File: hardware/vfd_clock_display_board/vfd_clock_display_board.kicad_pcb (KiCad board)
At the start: 2 copper layers, 124.9 x 94.6 mm, 96 parts, among them J1 Conn_01x12_Pin, Q1 MMDT5551, Q10 2N3906, Q11 2N3906, Q12 2N3906, Q13 MMDT5551, Q14 MMDT5551, Q15 2N3906, Q16 2N3906, Q17 2N3906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

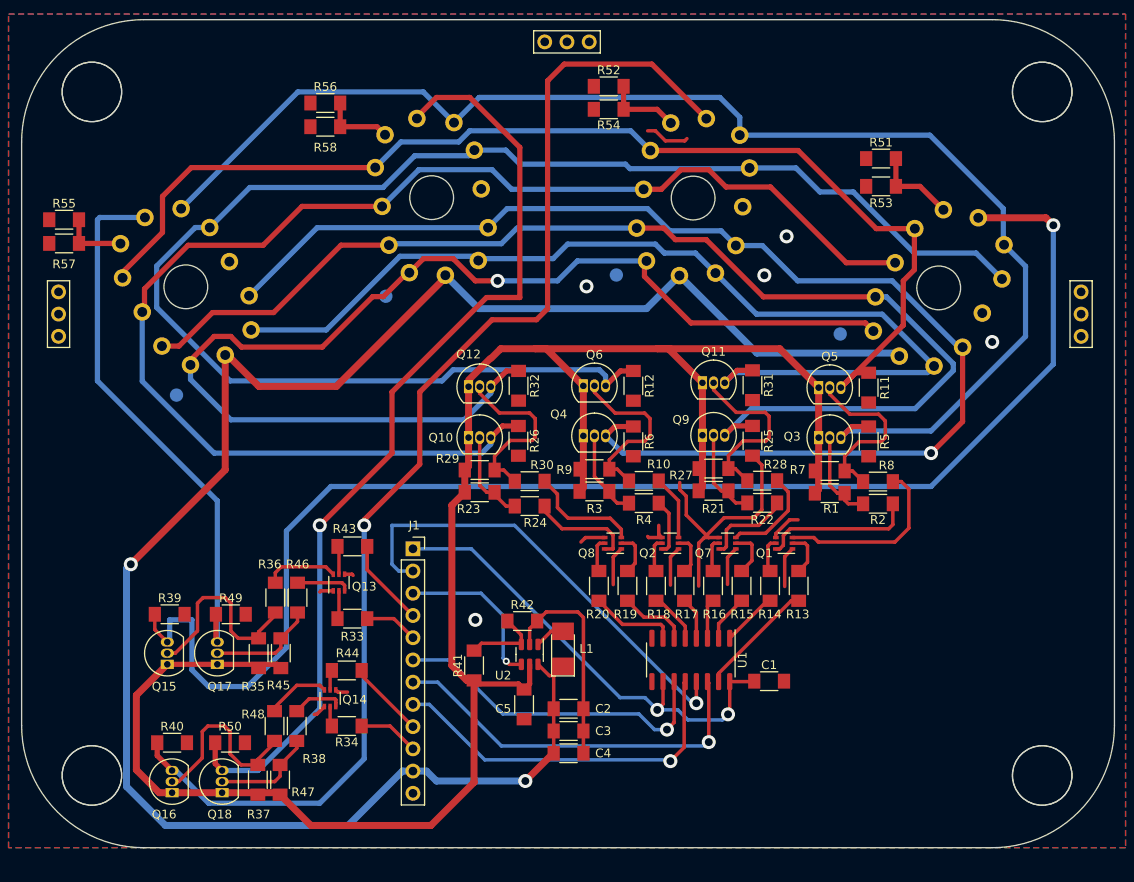
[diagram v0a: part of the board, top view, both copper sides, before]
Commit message: Add PCF version of main board, add test pads to display board
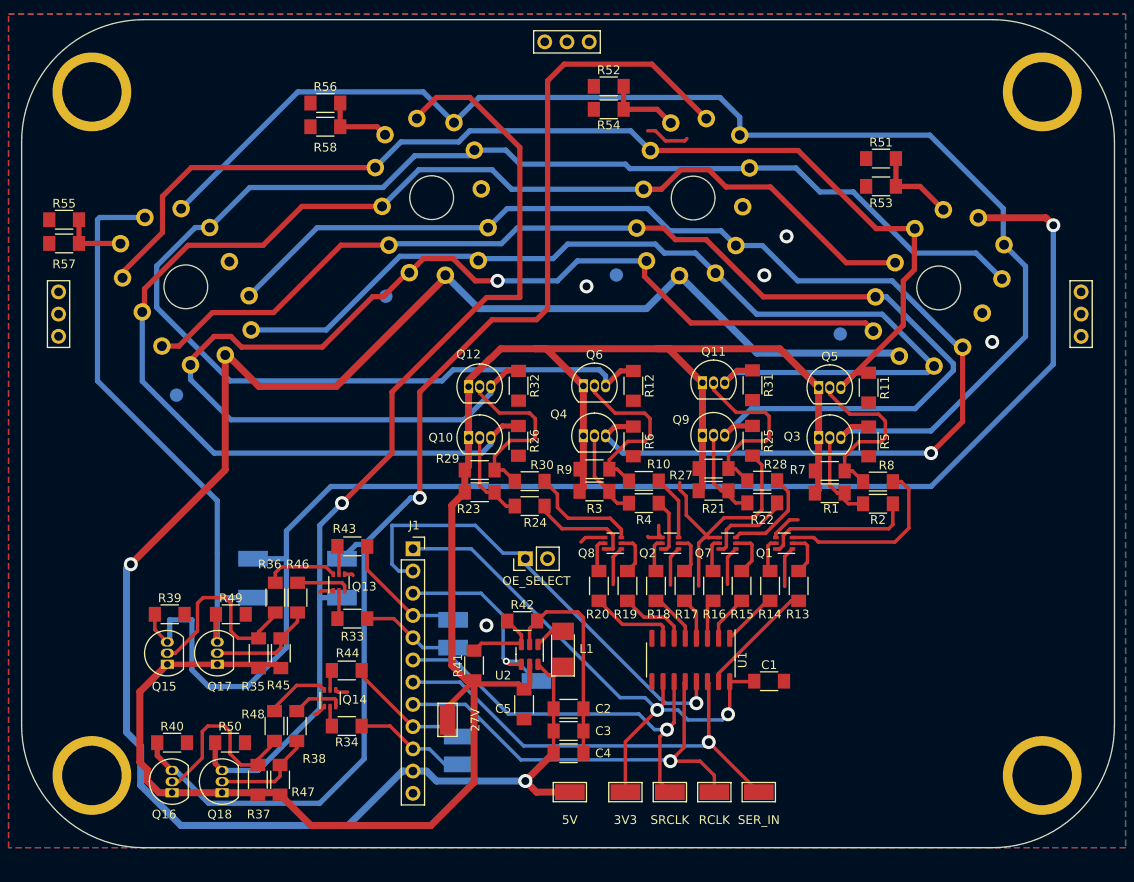
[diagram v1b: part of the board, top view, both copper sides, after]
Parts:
- added 27V: TestPoint_Keystone_5015_Micro-Minature, TestPoint:TestPoint_Keystone_5015_Micro-Minature, F.Cu at (139.1, 135.3)
- added 3V3: TestPoint_Keystone_5015_Micro-Minature, TestPoint:TestPoint_Keystone_5015_Micro-Minature, F.Cu at (159.4, 143.5)
- added 5V: TestPoint_Keystone_5015_Micro-Minature, TestPoint:TestPoint_Keystone_5015_Micro-Minature, F.Cu at (153.0, 143.5)
- added OE_SELECT: Conn_01x02_Pin, Connector_PinHeader_2.54mm:PinHeader_1x02_P2.54mm_Vertical, F.Cu at (147.9, 116.8)
- added RCLK: TestPoint_Keystone_5015_Micro-Minature, TestPoint:TestPoint_Keystone_5015_Micro-Minature, F.Cu at (169.5, 143.5)
- added SER_IN: TestPoint_Keystone_5015_Micro-Minature, TestPoint:TestPoint_Keystone_5015_Micro-Minature, F.Cu at (174.6, 143.5)
- added SRCLK: TestPoint_Keystone_5015_Micro-Minature, TestPoint:TestPoint_Keystone_5015_Micro-Minature, F.Cu at (164.5, 143.5)
- added TLV_EN: TestPoint_Keystone_5015_Micro-Minature, TestPoint:TestPoint_Keystone_5015_Micro-Minature, B.Cu at (149.2, 130.8)
- added VFD0_EN: TestPoint_Keystone_5015_Micro-Minature, TestPoint:TestPoint_Keystone_5015_Micro-Minature, B.Cu at (139.7, 127.0)
- added VFD0_GRID: TestPoint_Keystone_5015_Micro-Minature, TestPoint:TestPoint_Keystone_5015_Micro-Minature, B.Cu at (116.8, 116.8)
- added VFD1_EN: TestPoint_Keystone_5015_Micro-Minature, TestPoint:TestPoint_Keystone_5015_Micro-Minature, B.Cu at (139.7, 123.8)
- added VFD1_EN: TestPoint_Keystone_5015_Micro-Minature, TestPoint:TestPoint_Keystone_5015_Micro-Minature, B.Cu at (140.3, 137.2)
- added VFD1_EN: TestPoint_Keystone_5015_Micro-Minature, TestPoint:TestPoint_Keystone_5015_Micro-Minature, B.Cu at (140.3, 140.3)
- added VFD1_GRID: TestPoint_Keystone_5015_Micro-Minature, TestPoint:TestPoint_Keystone_5015_Micro-Minature, B.Cu at (116.8, 121.3)
- added VFD2_GRID: TestPoint_Keystone_5015_Micro-Minature, TestPoint:TestPoint_Keystone_5015_Micro-Minature, B.Cu at (127.0, 116.8)
- added VFD3_GRID: TestPoint_Keystone_5015_Micro-Minature, TestPoint:TestPoint_Keystone_5015_Micro-Minature, B.Cu at (127.0, 121.3)
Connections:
- ? pad : (no net) -> PWR_GND (x4)
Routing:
- net PWR_3V3: track 54.5 -> 65.4 mm
- net /SER_IN: track 44.0 -> 52.1 mm
- net /SRCLK: track 38.1 -> 46.1 mm
- net /RCLK: track 41.9 -> 48.9 mm
- net /VFD2_EN: track 6.94 -> 12.9 mm
- net /VFD3_EN: track 8.85 -> 14.5 mm
- net 27V: track 221.2 -> 226.7 mm
- net /VFD0_EN: track 6.13 -> 11.2 mm
- net /VFD1_EN: track 10.1 -> 14.9 mm
- net PWR_5V: track 212.4 -> 217.0 mm
- net /TLV_EN: track 18.6 -> 23.0 mm
- net /VFD1_GRID: track 62.7 -> 66.8 mm
- net /VFD2_GRID: track 140.1 -> 143.9 mm
- net /VFD0_GRID: track 161.7 -> 165.5 mm
- net /VFD3_GRID: track 108.6 -> 111.2 mm
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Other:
- outline, holes or cut-outs redrawn

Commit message: start redesigning display board
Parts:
- added C6: 1uF, Fab:C_1206, F.Cu at (232.6, 120.1)
- added C7: 1uF, Fab:C_1206, F.Cu at (232.6, 123.5)
- added C8: 1uF, Fab:C_1206, F.Cu at (232.6, 126.8)
- added C9: 1uF, Fab:C_1206, F.Cu at (232.6, 130.2)
- added J3: Conn_PinHeader_1x03_P2.54mm_Horizontal_SMD, fab:PinHeader_1x03_P2.54mm_Horizontal_SMD, F.Cu at (227.6, 96.5)
- added J4: Conn_01x10_MountingPin, Connector_FFC-FPC:Hirose_FH12-10S-0.5SH_1x10-1MP_P0.50mm_Horizontal, F.Cu at (204.3, 116.2)
- added U3: LED_ADDR_Worldsemi_WS2812B, Fab:LED_RGB_CreeLED_CLV1A-FKB, F.Cu at (136.4, 71.0)
- added U4: LED_ADDR_Worldsemi_WS2812B, Fab:LED_RGB_CreeLED_CLV1A-FKB, F.Cu at (226.0, 120.7)
- added U5: LED_ADDR_Worldsemi_WS2812B, Fab:LED_RGB_CreeLED_CLV1A-FKB, F.Cu at (226.0, 125.0)
- added U6: LED_ADDR_Worldsemi_WS2812B, Fab:LED_RGB_CreeLED_CLV1A-FKB, F.Cu at (226.0, 129.4)
- VFD1, VFD2, VFD3, VFD4: footprint VFD:IV-22 -> VFD:IV-22 - Pin
- renumbered OE_SELECT to J2
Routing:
- net /VFD_F: track 173.6 -> 168.4 mm

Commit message: Further hardware redesign
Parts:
- removed J4: Conn_01x10_MountingPin, Connector_FFC-FPC:Hirose_FH12-10S-0.5SH_1x10-1MP_P0.50mm_Horizontal
- added D1: LED_1206, fab:LED_1206, F.Cu at (113.7, 122.3)
- added D2: LED_1206, fab:LED_1206, F.Cu at (102.8, 121.3)
- added D3: LED_1206, fab:LED_1206, F.Cu at (102.9, 113.7)
- added R59: 5.1K, Fab:R_1206, F.Cu at (116.2, 122.3)
- added R60: 5.1K, Fab:R_1206, F.Cu at (102.8, 123.8)
- added R61: 5.1K, Fab:R_1206, F.Cu at (102.8, 116.3)
- J1: value Conn_01x12_Pin -> Conn_01x10_MountingPin; footprint Connector_PinSocket_2.54mm:PinSocket_1x12_P2.54mm_Vertical -> Connector_FFC-FPC:Molex_200528-0100_1x10-1MP_P1.00mm_Horizontal
- L1: footprint Fab:L_1210 -> Inductor_SMD:L_Changjiang_FNR6045S
- moved J3 132.1 mm to (96.7, 114.9), turned to 180 degrees
- moved TLV_EN 97.1 mm to (54.0, 111.8)
- moved VFD1_EN 93.5 mm to (48.3, 104.1)
- moved VFD1_EN 92.0 mm to (48.9, 130.2)
- moved VFD1_EN 91.4 mm to (49.5, 126.4)
- moved VFD0_EN 87.3 mm to (54.6, 107.3)
- moved VFD2_GRID 78.5 mm to (48.9, 109.2)
- moved VFD3_GRID 78.1 mm to (48.9, 121.9)
- moved C4 68.5 mm to (95.9, 101.1), turned to 180 degrees
- moved VFD1_GRID 68.1 mm to (48.9, 117.5)
- moved VFD0_GRID 67.4 mm to (49.5, 113.7)
- moved C3 65.8 mm to (95.9, 103.6), turned to 180 degrees
- moved C2 63.4 mm to (95.9, 106.1), turned to 180 degrees
- moved 3V3 56.2 mm to (107.3, 122.6), turned to -90 degrees
- moved 5V 54.0 mm to (107.3, 114.9), turned to -90 degrees
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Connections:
- J1 pad 1: PWR_3V3 -> /OE
- J1 pad 10: /VFD2_EN -> /LED_DIN
- J1 pad 2: /OE -> /TLV_EN
- J1 pad 3: /TLV_EN -> /VFD1_EN
- J1 pad 4: /VFD1_EN -> /VFD0_EN
- J1 pad 5: /VFD0_EN -> /SRCLK
- J1 pad 6: /SRCLK -> /SER_IN
- J1 pad 7: /SER_IN -> /RCLK
- J1 pad 8: /RCLK -> /VFD3_EN
- J1 pad 9: /VFD3_EN -> /VFD2_EN
- U3 pad 4: unconnected-(U3-DIN-Pad4) -> /LED_DIN
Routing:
- net /VFD0_GRID: track 165.5 -> 12.7 mm
- net /VFD2_GRID: track 143.9 -> 3.88 mm, vias 1 -> 0
- net /VFD3_GRID: track 111.2 -> 3.50 mm, vias 1 -> 0
- net PWR_5V: track 217.0 -> 146.3 mm, vias 2 -> 0
- net 27V: track 226.7 -> 162.6 mm
- net /VFD1_GRID: track 66.8 -> 3.24 mm
- net /OE: track 53.6 -> 2.47 mm
- net /SER_IN: track 52.1 -> 15.1 mm
- net /SRCLK: track 46.1 -> 13.8 mm
- net /RCLK: track 48.9 -> 16.8 mm
- net PWR_3V3: track 65.4 -> 40.2 mm
- net PWR_GND: track 92.8 -> 70.8 mm, vias 5 -> 4
- net /TLV_EN: track 23.0 -> 1.87 mm
- net /VFD1_EN: track 14.9 -> 0.00 mm
- net /VFD3_EN: track 14.5 -> 0.00 mm
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
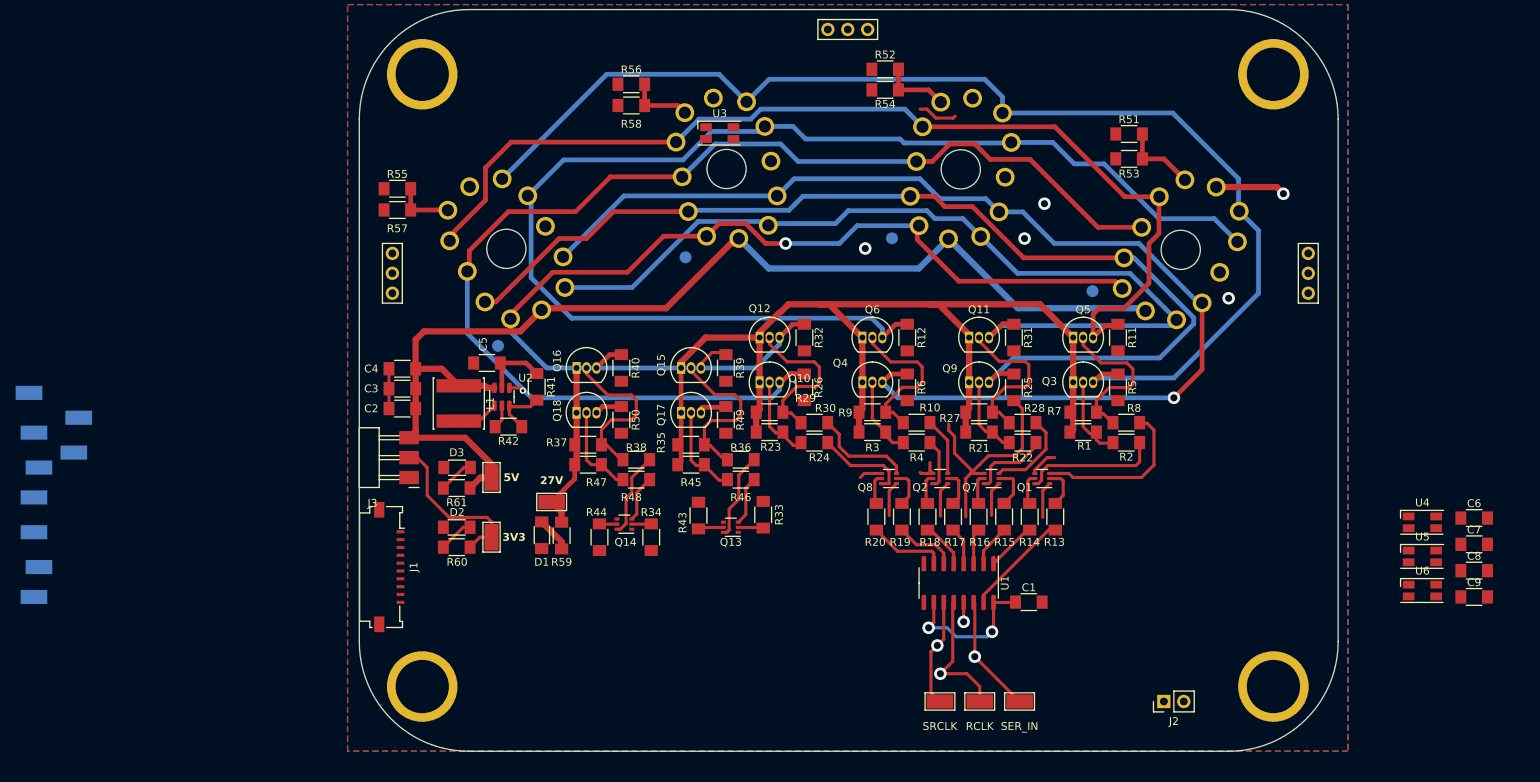
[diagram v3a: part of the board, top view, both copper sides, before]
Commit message: Move main board code to its own folder, update display board to match latest
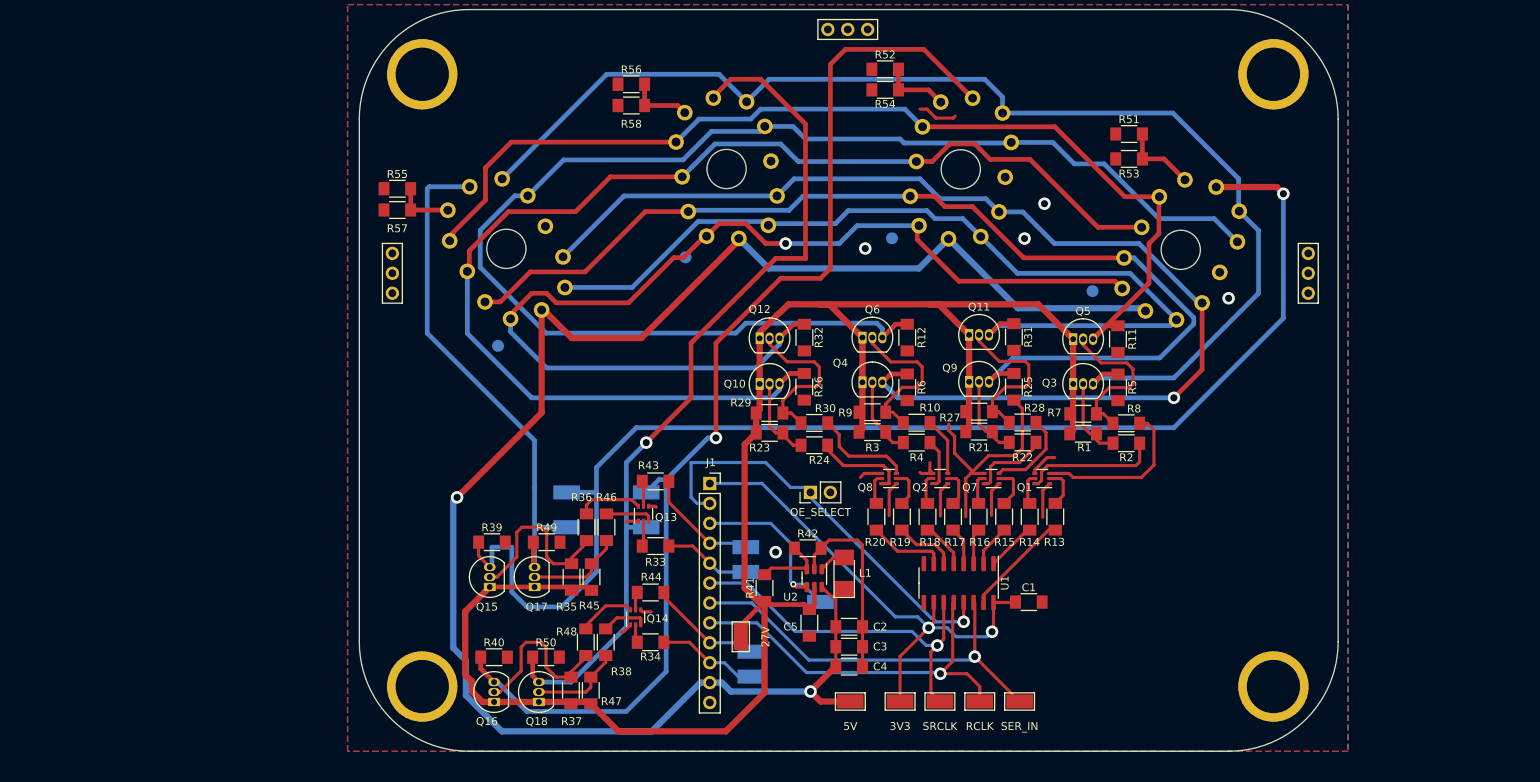
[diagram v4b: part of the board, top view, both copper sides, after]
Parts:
- removed C6, C7, C8, C9: 1uF, Fab:C_1206
- removed D1, D2, D3: LED_1206, fab:LED_1206
- removed J3: Conn_PinHeader_1x03_P2.54mm_Horizontal_SMD, fab:PinHeader_1x03_P2.54mm_Horizontal_SMD
- removed R59, R60, R61: 5.1K, Fab:R_1206
- removed U3, U4, U5, U6: LED_ADDR_Worldsemi_WS2812B, Fab:LED_RGB_CreeLED_CLV1A-FKB
- J1: value Conn_01x10_MountingPin -> Conn_01x12_Pin; footprint Connector_FFC-FPC:Molex_200528-0100_1x10-1MP_P1.00mm_Horizontal -> Connector_PinSocket_2.54mm:PinSocket_1x12_P2.54mm_Vertical
- L1: footprint Inductor_SMD:L_Changjiang_FNR6045S -> Fab:L_1210
- VFD1, VFD2, VFD3, VFD4: footprint VFD:IV-22 - Pin -> VFD:IV-22
- moved TLV_EN 97.1 mm to (149.2, 130.8)
- moved VFD1_EN 93.5 mm to (139.7, 123.8)
- moved VFD1_EN 92.0 mm to (140.3, 140.3)
- moved VFD1_EN 91.4 mm to (140.3, 137.2)
- moved VFD0_EN 87.3 mm to (139.7, 127.0)
- moved VFD2_GRID 78.5 mm to (127.0, 116.8)
- moved VFD3_GRID 78.1 mm to (127.0, 121.3)
- moved C4 68.5 mm to (152.9, 139.1), turned to 0 degrees
- moved VFD1_GRID 68.1 mm to (116.8, 121.3)
- moved VFD0_GRID 67.4 mm to (116.8, 116.8)
- moved C3 65.8 mm to (152.9, 136.5), turned to 0 degrees
- moved C2 63.4 mm to (152.9, 134.0), turned to 0 degrees
- moved 3V3 56.2 mm to (159.4, 143.5), turned to 0 degrees
- moved 5V 54.0 mm to (153.0, 143.5), turned to 0 degrees
- moved L1 53.7 mm to (152.3, 127.1), turned to 90 degrees
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- renumbered J2 to OE_SELECT
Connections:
- J1 pad 1: /OE -> PWR_3V3
- J1 pad 10: /LED_DIN -> /VFD2_EN
- J1 pad 2: /TLV_EN -> /OE
- J1 pad 3: /VFD1_EN -> /TLV_EN
- J1 pad 4: /VFD0_EN -> /VFD1_EN
- J1 pad 5: /SRCLK -> /VFD0_EN
- J1 pad 6: /SER_IN -> /SRCLK
- J1 pad 7: /RCLK -> /SER_IN
- J1 pad 8: /VFD3_EN -> /RCLK
- J1 pad 9: /VFD2_EN -> /VFD3_EN
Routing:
- net /VFD0_GRID: track 12.7 -> 165.5 mm
- net /VFD2_GRID: track 3.88 -> 143.9 mm, vias 0 -> 1
- net /VFD3_GRID: track 3.50 -> 111.2 mm, vias 0 -> 1
- net PWR_5V: track 146.3 -> 217.0 mm, vias 0 -> 2
- net 27V: track 162.6 -> 226.7 mm
- net /VFD1_GRID: track 3.24 -> 66.8 mm
- net /OE: track 2.47 -> 53.6 mm
- net /SER_IN: track 15.1 -> 52.1 mm
- net /SRCLK: track 13.8 -> 46.1 mm
- net /RCLK: track 16.8 -> 48.9 mm
- net PWR_3V3: track 40.2 -> 65.4 mm
- net PWR_GND: track 70.8 -> 92.8 mm, vias 4 -> 5
- net /TLV_EN: track 1.87 -> 23.0 mm
- net /VFD1_EN: track 0.00 -> 14.9 mm
- net /VFD3_EN: track 0.00 -> 14.5 mm
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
